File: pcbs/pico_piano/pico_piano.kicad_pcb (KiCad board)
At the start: 2 copper layers, 73 x 57.5 mm, 22 parts, among them U1 Pico

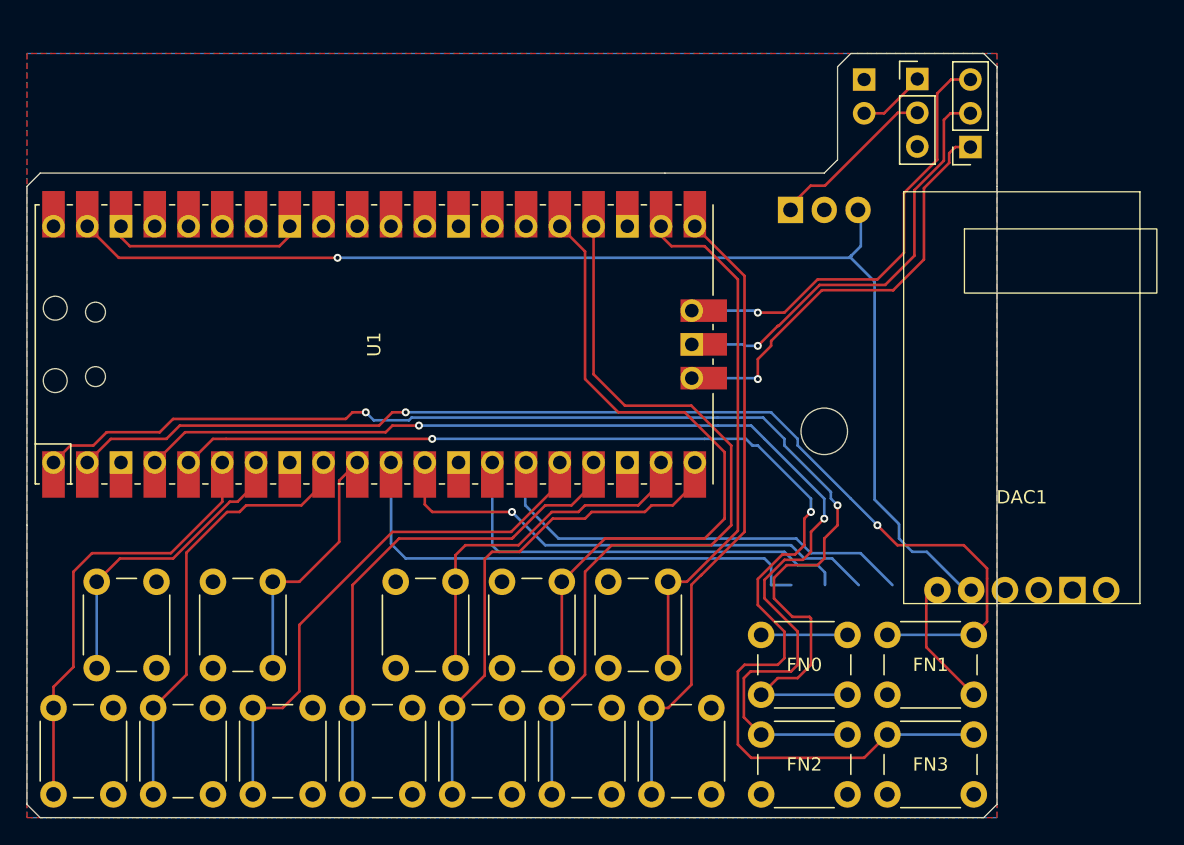
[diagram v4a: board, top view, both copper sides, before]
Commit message: Update Pico Piano PCB components
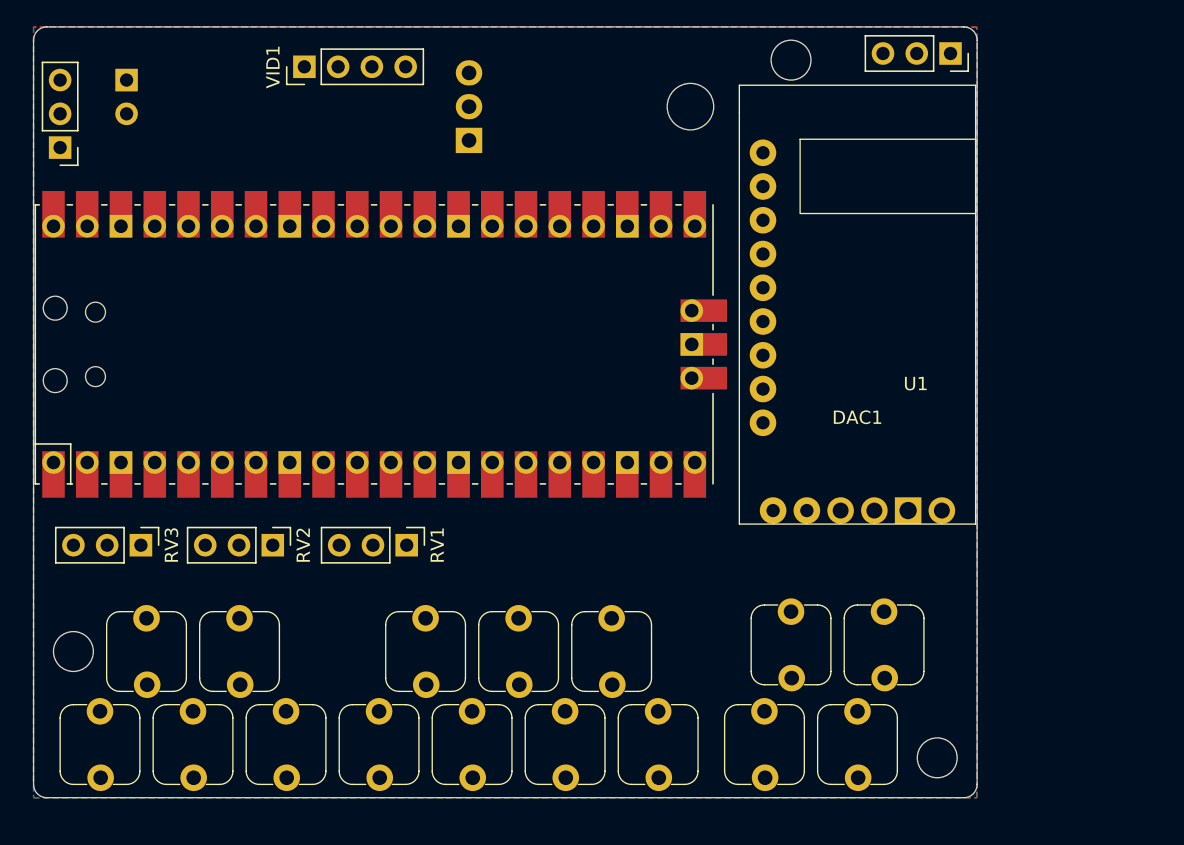
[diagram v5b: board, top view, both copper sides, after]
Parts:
- removed NOTE_A1, NOTE_AIS1, NOTE_B1, NOTE_C1, NOTE_CIS1, NOTE_D1, NOTE_DIS1, NOTE_E1, NOTE_F1, NOTE_FIS1, NOTE_G1, NOTE_GIS1: SW_Push, Button_Switch_THT:SW_PUSH_6mm
- added A1: SW_Push, rytmos:KAILH_MUTE, F.Cu at (140.0, 77.0)
- added AIS1: SW_Push, rytmos:KAILH_MUTE, F.Cu at (143.5, 70.0)
- added B1: SW_Push, rytmos:KAILH_MUTE, F.Cu at (147.0, 77.0)
- added C1: SW_Push, rytmos:KAILH_MUTE, F.Cu at (105.0, 77.0)
- added CIS1: SW_Push, rytmos:KAILH_MUTE, F.Cu at (108.5, 70.0)
- added D1: SW_Push, rytmos:KAILH_MUTE, F.Cu at (112.0, 77.0)
- added DIS1: SW_Push, rytmos:KAILH_MUTE, F.Cu at (115.5, 70.0)
- added E1: SW_Push, rytmos:KAILH_MUTE, F.Cu at (119.0, 77.0)
- added F1: SW_Push, rytmos:KAILH_MUTE, F.Cu at (126.0, 77.0)
- added FIS1: SW_Push, rytmos:KAILH_MUTE, F.Cu at (129.5, 70.0)
- added G1: SW_Push, rytmos:KAILH_MUTE, F.Cu at (133.0, 77.0)
- added GIS1: SW_Push, rytmos:KAILH_MUTE, F.Cu at (136.5, 70.0)
- added RV1: R_Potentiometer, Connector_PinHeader_2.54mm:PinHeader_1x03_P2.54mm_Vertical, F.Cu at (131.1, 59.0)
- added RV2: R_Potentiometer, Connector_PinHeader_2.54mm:PinHeader_1x03_P2.54mm_Vertical, F.Cu at (121.0, 59.0)
- added RV3: R_Potentiometer, Connector_PinHeader_2.54mm:PinHeader_1x03_P2.54mm_Vertical, F.Cu at (111.1, 59.0)
- added VID1: I2C, Connector_PinHeader_2.54mm:PinHeader_1x04_P2.54mm_Vertical, F.Cu at (123.4, 23.0)
- FN0, FN1, FN2, FN3: footprint Button_Switch_THT:SW_PUSH_6mm -> rytmos:KAILH_MUTE
- moved ON/OFF1 64.7 mm to (105.0, 29.1), turned to 180 degrees
- moved 9V_BAT1 55.5 mm to (110.0, 24.0)
- moved POWER1 24.7 mm to (135.8, 28.5), turned to 90 degrees
- moved DAC1 13.7 mm to (165.0, 57.4)
- moved FN0 7.29 mm to (157.0, 69.5), turned to 0 degrees
- moved DBG1 7.20 mm to (172.0, 22.0), turned to -90 degrees
- moved FN3 6.45 mm to (162.0, 77.0)
- moved FN1 4.96 mm to (164.0, 69.5)
- moved FN2 4.65 mm to (155.0, 77.0)
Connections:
- U1 pad 26: unconnected-(U1-GPIO20-Pad26) -> /VID_SDA
- U1 pad 27: unconnected-(U1-GPIO21-Pad27)_1 -> /VID_SCK
- U1 pad 31: unconnected-(U1-GPIO26_ADC0-Pad31) -> /ADC0
- U1 pad 32: unconnected-(U1-GPIO27_ADC1-Pad32)_1 -> /ADC1
- U1 pad 34: unconnected-(U1-GPIO28_ADC2-Pad34)_1 -> /ADC2
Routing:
- net /FN3: track 92.8 -> 0.00 mm, vias 2 -> 0
- net /FN0: track 92.6 -> 0.00 mm, vias 2 -> 0
- net +5V: track 91.7 -> 0.00 mm, vias 1 -> 0
- net /FN1: track 86.3 -> 0.00 mm, vias 2 -> 0
- net /FN2: track 85.8 -> 0.00 mm, vias 2 -> 0
- net /A: track 60.0 -> 0.00 mm
- net /GIS: track 50.8 -> 0.00 mm
- net /B: track 47.9 -> 0.00 mm
- net /E: track 41.1 -> 0.00 mm
- net /AIS: track 39.4 -> 0.00 mm
- net /F: track 38.6 -> 0.00 mm
- net /G: track 38.4 -> 0.00 mm
- net /SCK: track 38.4 -> 0.00 mm
- net /DIN: track 38.3 -> 0.00 mm, vias 1 -> 0
- net Net-(DBG1-Pin_3): track 33.9 -> 0.00 mm, vias 1 -> 0
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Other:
- board size 73 x 57.5 mm -> 71 x 58 mm
- board text added: "Pico Piano v0.2"
- board text removed: "Pico Piano v0.1"

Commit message: Route tracks on pico piano v0.2
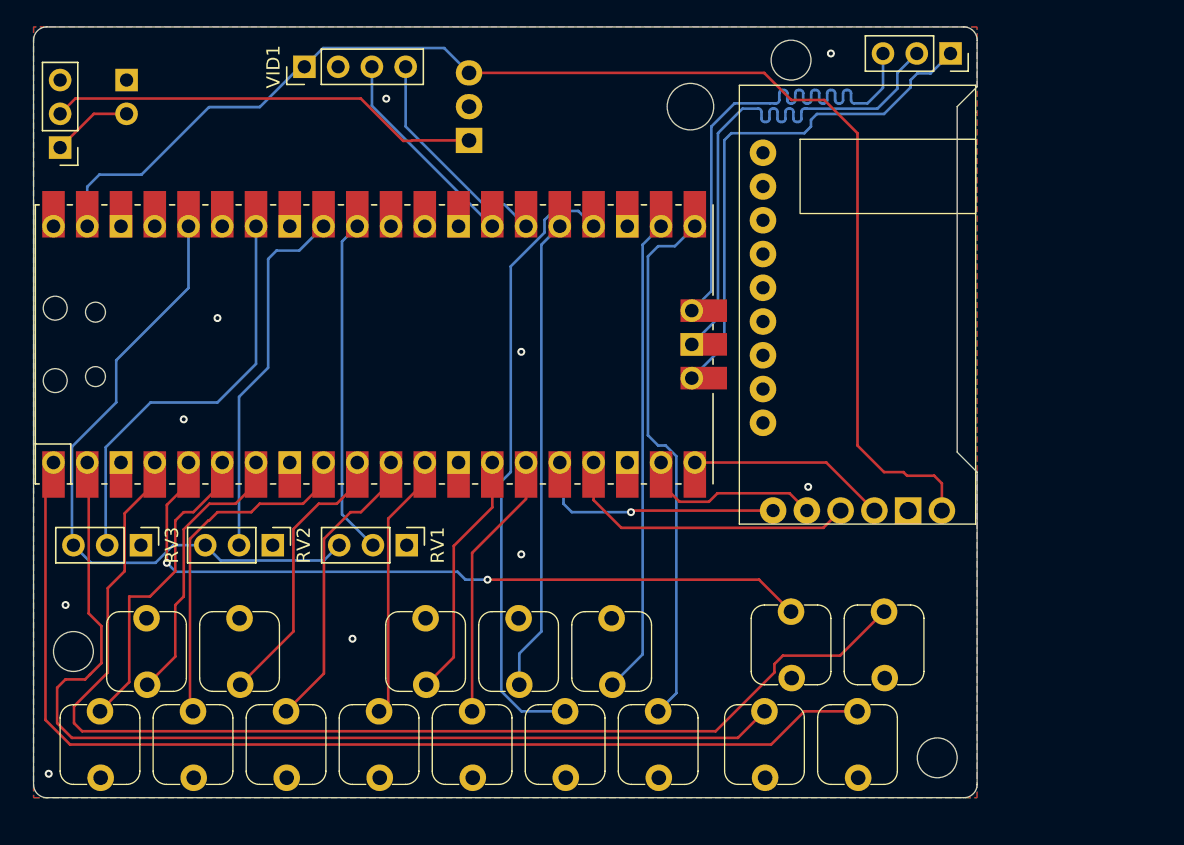
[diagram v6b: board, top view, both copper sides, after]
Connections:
- RV1 pad 1: +3V3 -> GND
- RV1 pad 3: GND -> +3V3
- RV2 pad 1: +3V3 -> GND
- RV2 pad 3: GND -> +3V3
- RV3 pad 1: +3V3 -> GND
- RV3 pad 3: GND -> +3V3
- U1 pad 1: /FN0 -> /FN3
- U1 pad 11: /SCK -> /E
- U1 pad 12: /DIN -> /F
- U1 pad 14: /BCK -> /FIS
- U1 pad 15: /LRCK -> /G
- U1 pad 16: /E -> /SCK
- U1 pad 17: /F -> /DIN
- U1 pad 19: /FIS -> /BCK
- U1 pad 2: /FN1 -> /FN2
- U1 pad 20: /G -> /LRCK
- U1 pad 36: /3V3 -> +3V3
- U1 pad 4: /FN2 -> /FN1
- U1 pad 5: /FN3 -> /FN0
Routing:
- net +5V: track 0.00 -> 101.0 mm
- net /FN1: track 0.00 -> 87.4 mm
- net /FN3: track 0.00 -> 82.5 mm
- net /FN2: track 0.00 -> 76.8 mm
- net /FN0: track 0.00 -> 56.7 mm, vias 0 -> 2
- net +3V3: track 0.00 -> 49.7 mm
- net /A: track 0.00 -> 46.7 mm
- net /B: track 0.00 -> 40.5 mm
- net Net-(DBG1-Pin_2): track 0.00 -> 39.5 mm
- net Net-(DBG1-Pin_1): track 0.00 -> 39.3 mm
- net Net-(DBG1-Pin_3): track 0.00 -> 38.9 mm
- net /AIS: track 0.00 -> 36.0 mm
- net /GIS: track 0.00 -> 35.8 mm
- net Net-(POWER1-VI): track 0.00 -> 32.6 mm
- net /ADC2: track 0.00 -> 31.7 mm
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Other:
- outline, holes or cut-outs redrawn

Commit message: Clean up most synths
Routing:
- net /FN2: track 76.8 -> 75.6 mm
- net /FN1: track 87.4 -> 88.1 mm

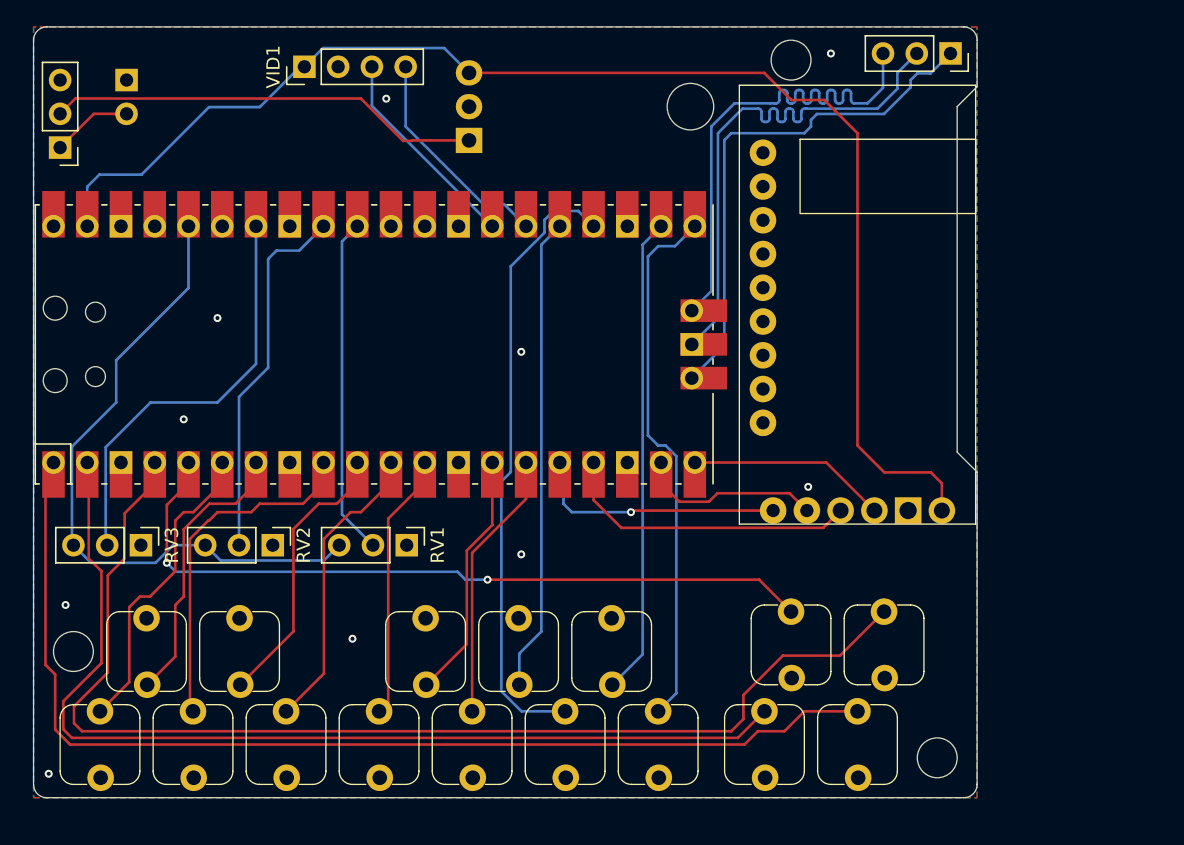
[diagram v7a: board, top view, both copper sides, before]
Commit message: Order v0.2 of pico piano PCB
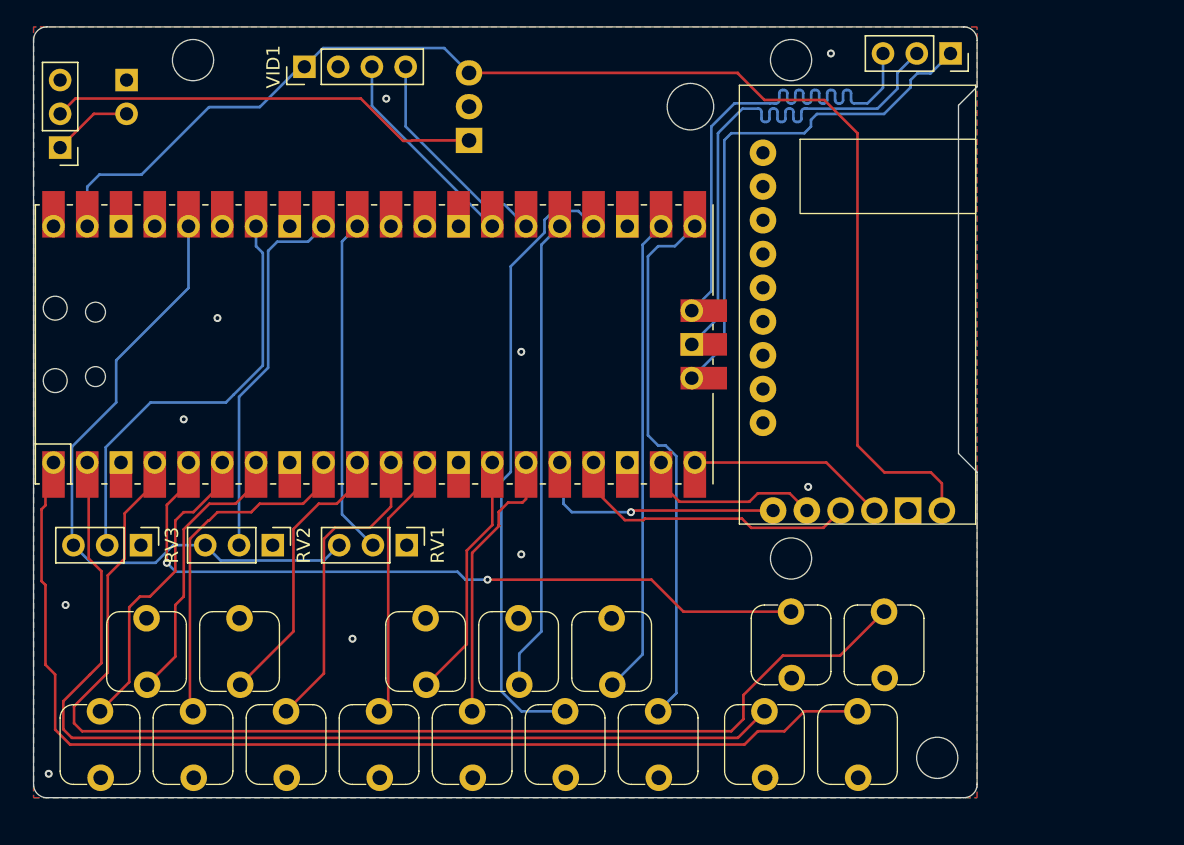
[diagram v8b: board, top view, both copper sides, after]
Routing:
- net /E: track 22.4 -> 23.5 mm
- net /ADC2: track 31.7 -> 32.5 mm
- net /G: track 20.4 -> 21.1 mm
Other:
- outline, holes or cut-outs redrawn
